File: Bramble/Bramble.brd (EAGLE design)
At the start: 84.8 x 55.9 mm, 17 parts

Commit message: 2x 2 port usb
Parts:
- removed PWR1, PWR2, PWR3, PWR4: 614004134726, Wurth_Connectors_WR-USB:614004134726
- added J3, J4: 5787745-1, 5787745-1:TE_5787745-1
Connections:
- removed net N$1: C1.+, FL1.1, PWR1.1
- removed net N$2: C2.+, FL2.1, PWR2.1
- removed net N$3: C4.+, FL4.1, PWR4.1
- removed net N$4: C3.+, FL3.1, PWR3.1
- new net 5VOUT1: C1.+, FL1.1, J3.1
- new net 5VOUT2: C2.+, FL2.1, J3.5
- new net 5VOUT3: C3.+, FL3.1, J4.1
- new net 5VOUT4: C4.+, FL4.1, J4.5
- net GND: now also J3.4, J3.8, J3.S1, J3.S2, J3.S3, J3.S4, J4.4, J4.8, J4.S1, J4.S2, J4.S3, J4.S4; no longer PWR1.4, PWR1.S1, PWR1.S2, PWR1.S3, PWR1.S4, PWR2.4, PWR2.S1, PWR2.S2, PWR2.S3, PWR2.S4, PWR3.4, PWR3.S1, PWR3.S2, PWR3.S3, PWR3.S4, PWR4.4, PWR4.S1, PWR4.S2, PWR4.S3, PWR4.S4
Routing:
- net N$3: track 30.9 -> 0.00 mm
- net N$4: track 29.1 -> 0.00 mm
- net N$2: track 26.5 -> 0.00 mm
- net N$1: track 25.4 -> 0.00 mm
- net 5VOUT4: track 0.00 -> 9.71 mm
- net 5VOUT3: track 0.00 -> 9.71 mm
- net 5VOUT2: track 0.00 -> 9.71 mm
- net 5VOUT1: track 0.00 -> 9.71 mm

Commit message: joined 1 and 2  aaand 3 and 4
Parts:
- removed J3, J4: 5787745-1, 5787745-1:TE_5787745-1
- added USB12, USB34: 5787745-1, 5787745-1:TE_5787745-1
- FL1, FL2, FL3, FL4: value BLM18PG121SH1D -> BLM18KG121TN1D
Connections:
- removed net 5VOUT1: C1.+, FL1.1, J3.1
- removed net 5VOUT2: C2.+, FL2.1, J3.5
- removed net 5VOUT3: C3.+, FL3.1, J4.1
- removed net 5VOUT4: C4.+, FL4.1, J4.5
- new net 5VOUT12: C1.+, C2.+, FL1.1, FL2.1, USB12.1, USB12.5
- new net 5VOUT34: C3.+, C4.+, FL3.1, FL4.1, USB34.1, USB34.5
- net GND: now also USB12.4, USB12.8, USB12.S1, USB12.S2, USB12.S3, USB12.S4, USB34.4, USB34.8, USB34.S1, USB34.S2, USB34.S3, USB34.S4; no longer J3.4, J3.8, J3.S1, J3.S2, J3.S3, J3.S4, J4.4, J4.8, J4.S1, J4.S2, J4.S3, J4.S4
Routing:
- net 5VOUT12: track 0.00 -> 23.2 mm
- net 5VOUT34: track 0.00 -> 22.4 mm
- net 5VOUT4: track 9.71 -> 0.00 mm
- net 5VOUT3: track 9.71 -> 0.00 mm
- net 5VOUT2: track 9.71 -> 0.00 mm
- net 5VOUT1: track 9.71 -> 0.00 mm
- added copper zone on layer 1, net 5VOUT12
- added copper zone on layer 1, net 5VOUT34

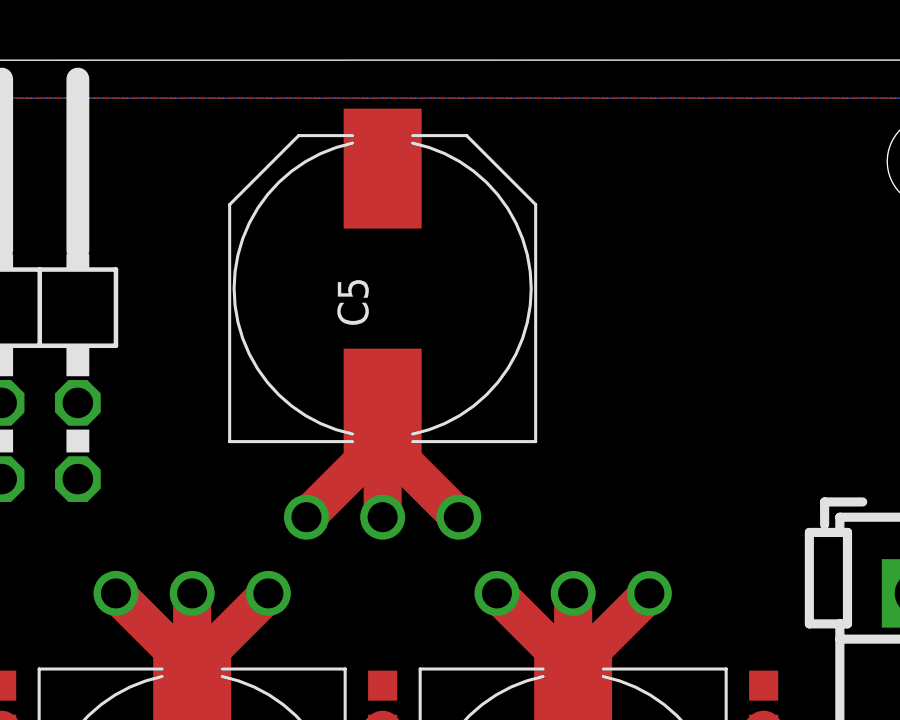
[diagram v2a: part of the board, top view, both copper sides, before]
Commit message: Moved capacitor
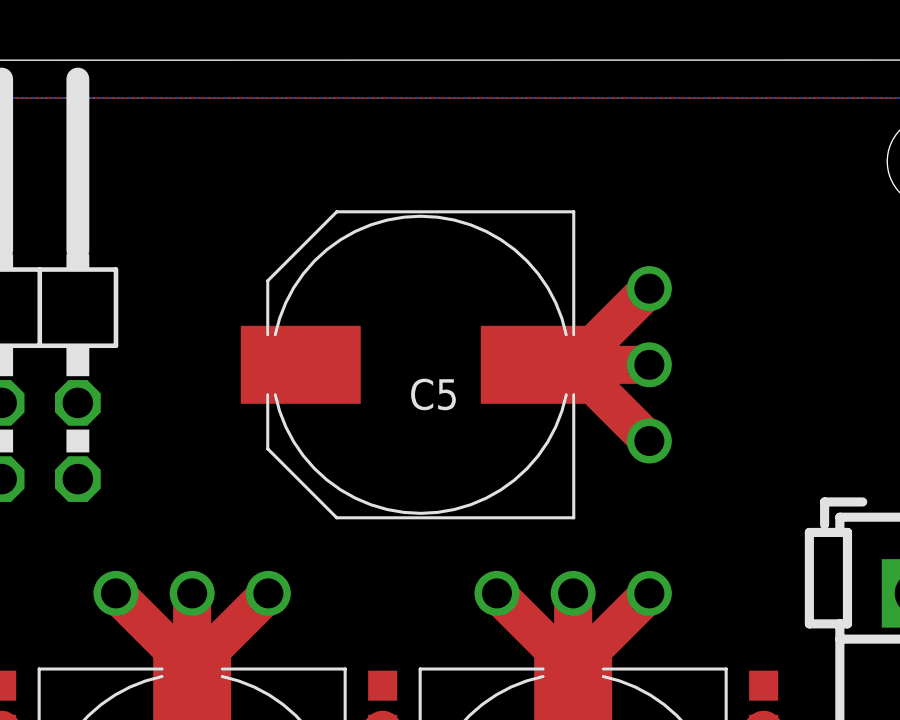
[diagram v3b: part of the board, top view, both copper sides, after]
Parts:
- moved C5 2.84 mm to (44.5, 45.7), turned to 180 degrees
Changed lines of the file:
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@@
 <attribute name="NAME" x="10.64" y="31.76" size="1.016" layer="25" rot="R270"/>
 </element>
-<element name="C5" library="cap-vishay-153clv" package="153CLV-1010" value="CPOL-1010" x="43.18" y="48.26" smashed="yes" rot="R90">
-<attribute name="NAME" x="42.7" y="46.98" size="1.016" layer="25" rot="R90"/>
+<element name="C5" library="cap-vishay-153clv" package="153CLV-1010" value="CPOL-1010" x="44.45" y="45.72" smashed="yes" rot="R180">
+<attribute name="NAME" x="45.73" y="45.24" size="1.016" layer="25" rot="R180"/>
 </element>
 <element name="FL1" library="BLM18PG121SH1D" package="BEADC1608X95N" value="BLM18KG121TN1D" x="55.88" y="34.29" smashed="yes" rot="R90">
@@
 <contactref element="FL4" pad="2"/>
 <contactref element="F1" pad="1"/>
-<wire x1="43.18" y1="35.025" x2="30.48" y2="35.025" width="0" layer="19" extent="1-1"/>
 </signal>
 <signal name="GND">
@@
 <via x="49.53" y="38.1" extent="1-16" drill="1"/>
 <via x="46.99" y="38.1" extent="1-16" drill="1"/>
-<via x="45.72" y="40.64" extent="1-16" drill="1"/>
-<via x="43.18" y="40.64" extent="1-16" drill="1"/>
-<via x="40.64" y="40.64" extent="1-16" drill="1"/>
+<via x="52.07" y="48.26" extent="1-16" drill="1"/>
+<via x="52.07" y="45.72" extent="1-16" drill="1"/>
+<via x="52.07" y="43.18" extent="1-16" drill="1"/>
 <wire x1="11.43" y1="34.48" x2="11.43" y2="38.1" width="1.27" layer="1"/>
 <wire x1="8.89" y1="38.1" x2="11.43" y2="35.56" width="1.27" layer="1"/>
@@
 <wire x1="39.37" y1="38.1" x2="36.83" y2="35.56" width="1.27" layer="1"/>
 <wire x1="36.83" y1="35.56" x2="36.83" y2="34.48" width="1.27" layer="1"/>
-<wire x1="43.18" y1="40.64" x2="43.18" y2="44.26" width="1.27" layer="1"/>
-<wire x1="40.64" y1="40.64" x2="43.18" y2="43.18" width="1.27" layer="1"/>
-<wire x1="45.72" y1="40.64" x2="43.18" y2="43.18" width="1.27" layer="1"/>
-<wire x1="43.18" y1="43.18" x2="43.18" y2="44.26" width="1.27" layer="1"/>
+<wire x1="52.07" y1="45.72" x2="48.45" y2="45.72" width="1.27" layer="1"/>
+<wire x1="52.07" y1="43.18" x2="49.53" y2="45.72" width="1.27" layer="1"/>
+<wire x1="52.07" y1="48.26" x2="49.53" y2="45.72" width="1.27" layer="1"/>
+<wire x1="49.53" y1="45.72" x2="48.45" y2="45.72" width="1.27" layer="1"/>
 <wire x1="49.53" y1="35.56" x2="49.53" y2="38.1" width="1.27" layer="1"/>
 <wire x1="46.99" y1="38.1" x2="49.53" y2="35.56" width="1.27" layer="1"/>

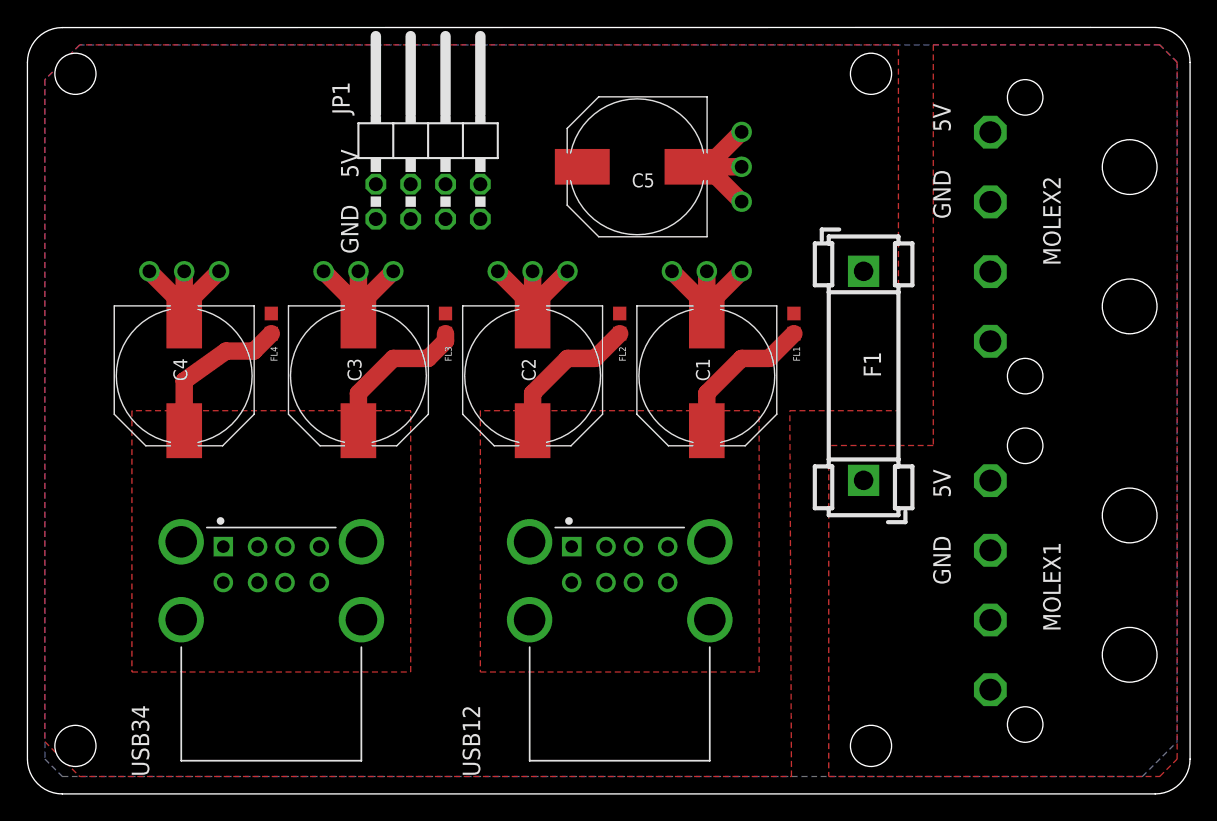
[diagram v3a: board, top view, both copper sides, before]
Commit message: Tweaked parts position
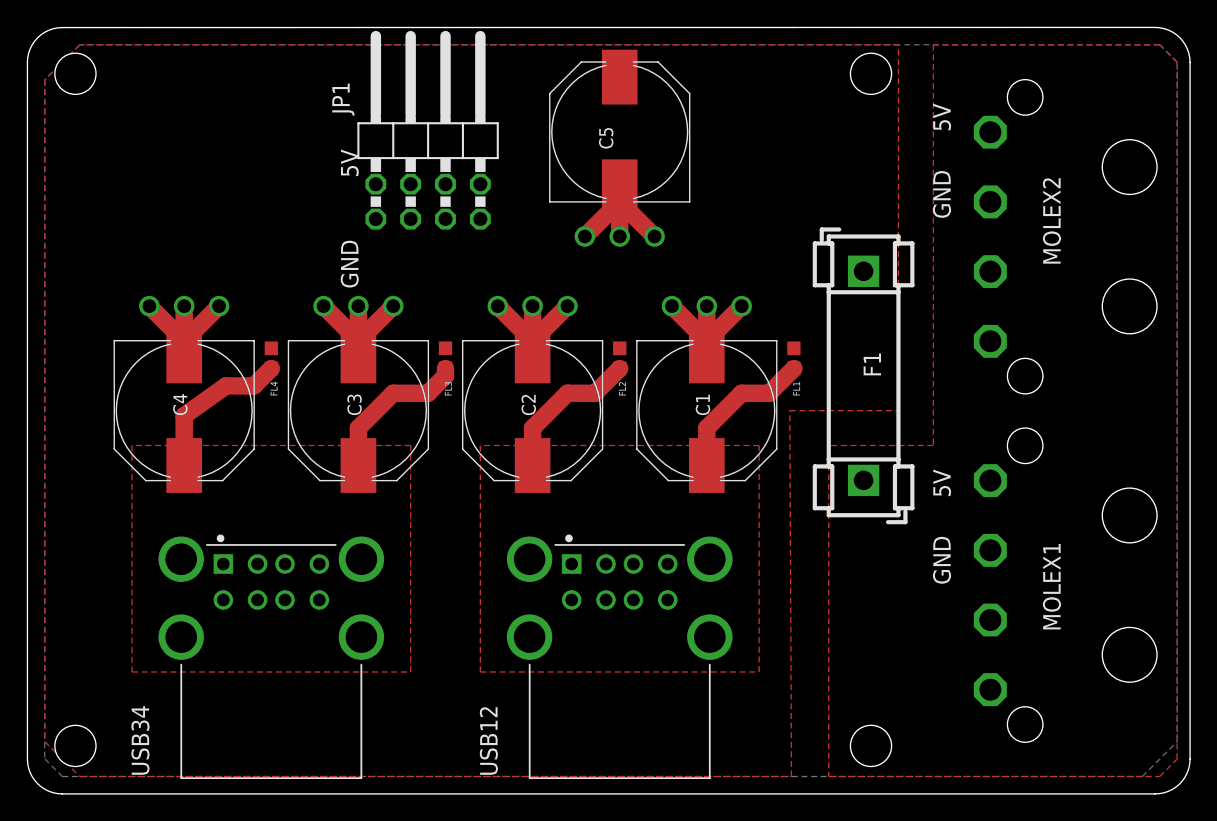
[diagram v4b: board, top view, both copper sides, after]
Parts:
- moved C5 2.84 mm to (43.2, 48.3), turned to 90 degrees
- moved C1 2.54 mm to (49.5, 27.9)
- moved C2 2.54 mm to (36.8, 27.9)
- moved C3 2.54 mm to (24.1, 27.9)
- moved C4 2.54 mm to (11.4, 27.9)
- moved FL1 2.54 mm to (55.9, 31.8)
- moved FL2 2.54 mm to (43.2, 31.8)
- moved FL3 2.54 mm to (30.5, 31.8)
- moved FL4 2.54 mm to (17.8, 31.8)
- moved USB12 1.27 mm to (43.2, 11.4)
- moved USB34 1.27 mm to (17.8, 11.4)
